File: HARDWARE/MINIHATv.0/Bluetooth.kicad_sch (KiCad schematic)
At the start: 0 parts

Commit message: added BT module and passives+xtals
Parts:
- added C24: 10n, symbol Device:C_Small
- added C25, C26, C27, C28, C29, C30: C_Small, symbol Device:C_Small
- added C31, C32, C33, C34, C35, C36: C, symbol Device:C
- added L1, L2: L, symbol Device:L
- added R26, R27: 4k7, symbol Device:R_Small
- added R28: 1K, symbol Device:R_Small
- added U6: BlueNRG-232NS, Library:VFQFPN-32_5x5_Pitch0.5mm, symbol RFLiB:BlueNRG-232N
- added Y2: 32kHz, symbol Device:Crystal_Small
- added Y3: 32MHz, symbol Device:Crystal_Small
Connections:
- new net: C29.2, U6.18 (FXTAL0), Y3.2
- new net: C27.2, C28.1, L2.1
- new net: R28.1, U6.29 (DIO13)
- new net: C25.1, C26.1, L1.1, U6.27 (SMPSFILT2)
- new net: L1.2, U6.26 (SMPSFILT1)
- new net: R27.2, U6.30 (DIO12)
- new net: C30.2, U6.17 (FXTAL1), Y3.1
- new net: C28.2, U6.22 (SXTAL1), Y2.1
- new net: C27.1, U6.23 (SXTAL0), Y2.2
- new net +3V3: C31.1, C32.1, C33.1, C34.1, R26.1, R27.1, U6.19 (VBAT2), U6.24 (VBAT1), U6.6 (VBAT3)
- new net BOOT: U6.4 (DIO7/BOOT)
- new net BT_RX: U6.3 (DIO8)
- new net BT_TX: U6.32 (DIO11)
- new net BT_VDD1V2: C35.1, C36.1, U6.28 (VDD1V2)
- new net BT_~RST: C24.1, R26.2, U6.25 (RESETN)
- new net GND: C24.2, C25.2, C26.2, C29.1, C30.1, C31.2, C32.2, C33.2, C34.2, C35.2, C36.2, L2.2, R28.2, U6.11 (DIO1), U6.12 (DIO0), U6.15 (ADC1), U6.16 (ADC2), U6.31 (TEST), U6.33 (GND), U6.5 (DIO6), U6.7 (DIO5), U6.8 (DIO4)
- no-connect marks 0 -> 6

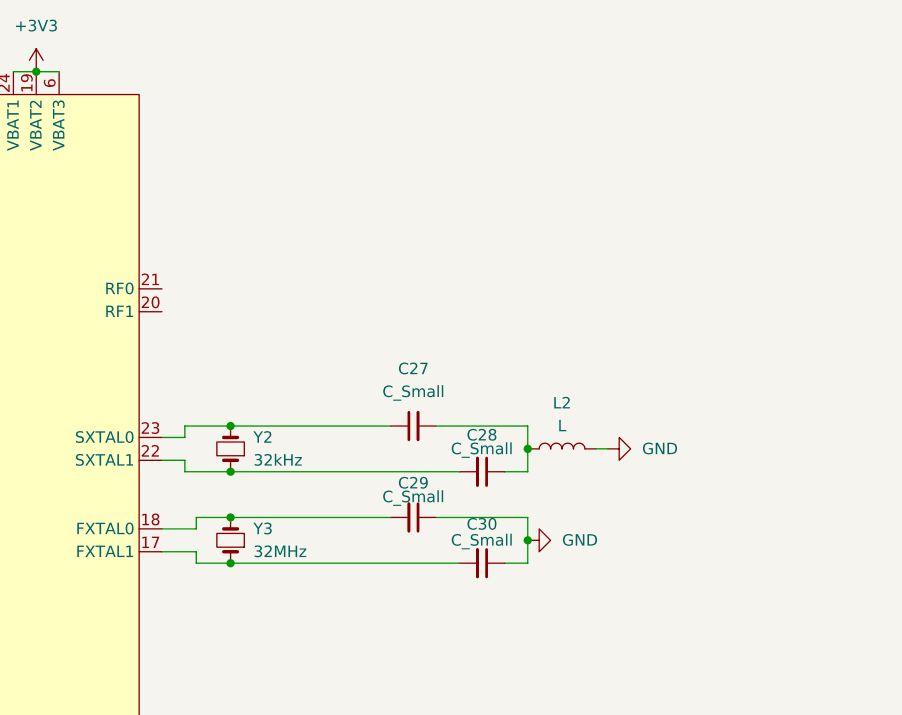
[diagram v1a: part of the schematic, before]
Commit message: passives and filter for BT antenna added to sch
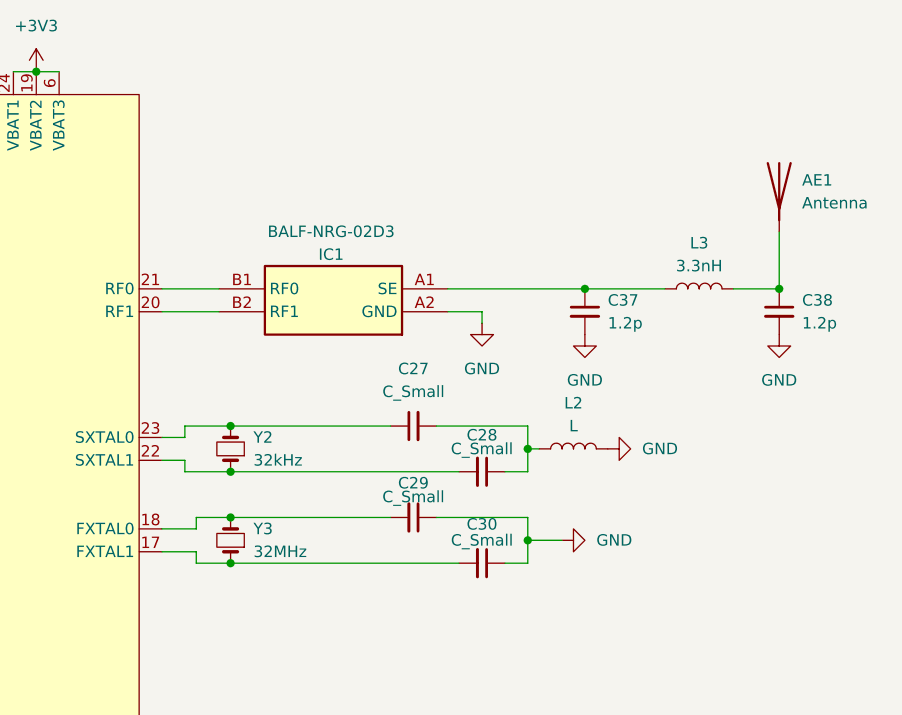
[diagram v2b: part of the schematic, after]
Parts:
- added AE1: Antenna, symbol Device:Antenna
- added C37, C38: 1.2p, Capacitor_SMD:C_0402_1005Metric, symbol Device:C_Small
- added IC1: BALF-NRG-02D3, BALFNRG02D3, symbol tmp:BALF-NRG-02D3
- added L3: 3.3nH, Inductor_SMD:L_0402_1005Metric, symbol Device:L
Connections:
- net GND: now also C37.2, C38.2, IC1.A2 (GND)
- net at U6.20 (RF1): now also IC1.B2 (RF1)
- net at U6.21 (RF0): now also IC1.B1 (RF0)
- new net: AE1.1 (A), C38.1, L3.2
- new net: C37.1, IC1.A1 (SE), L3.1
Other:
- moved on the sheet: L2

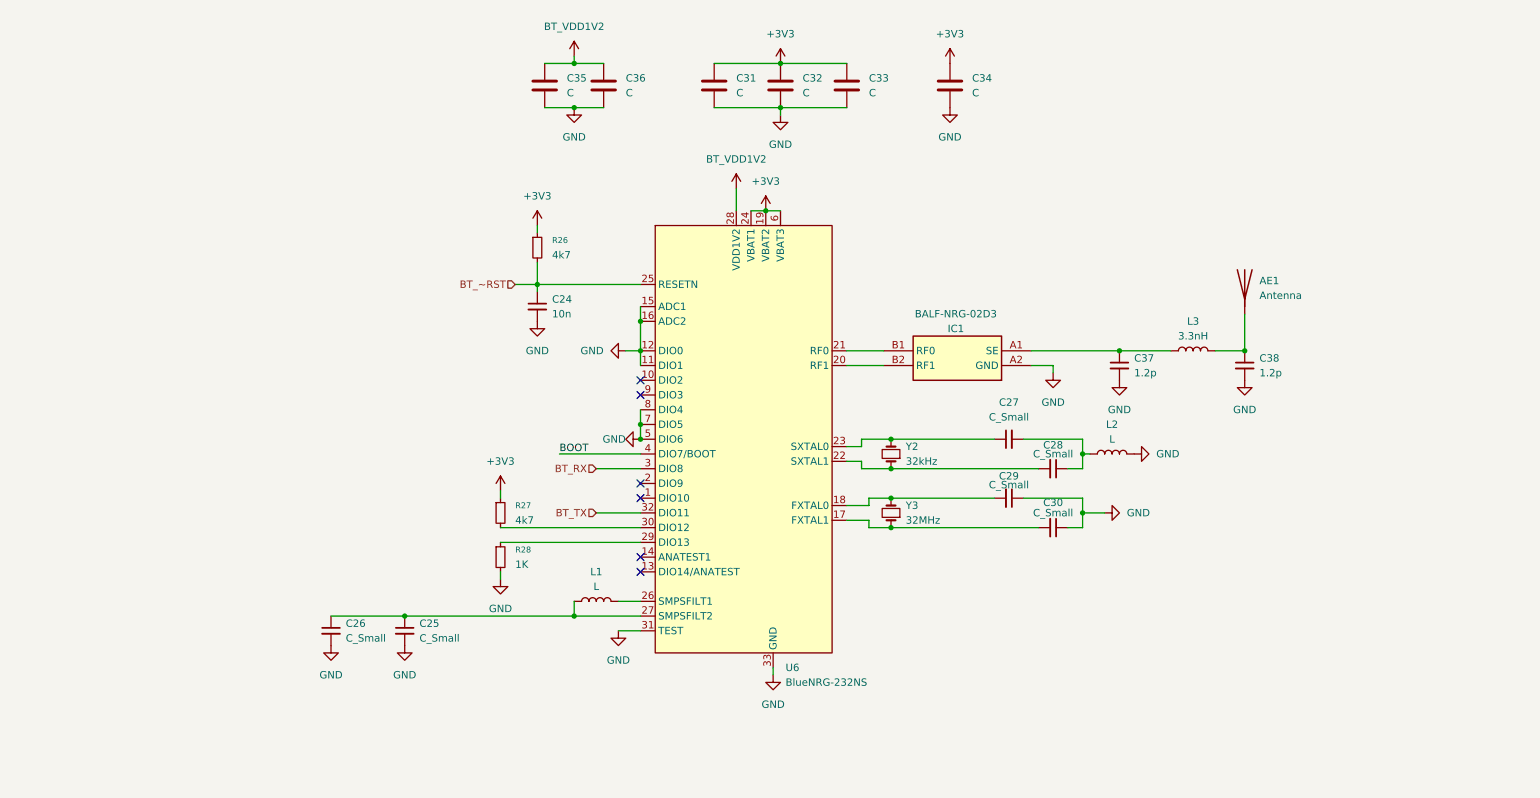
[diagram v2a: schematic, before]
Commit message: added bt chip filter valueas and xtal passives values, added antenna filter sources and footprint
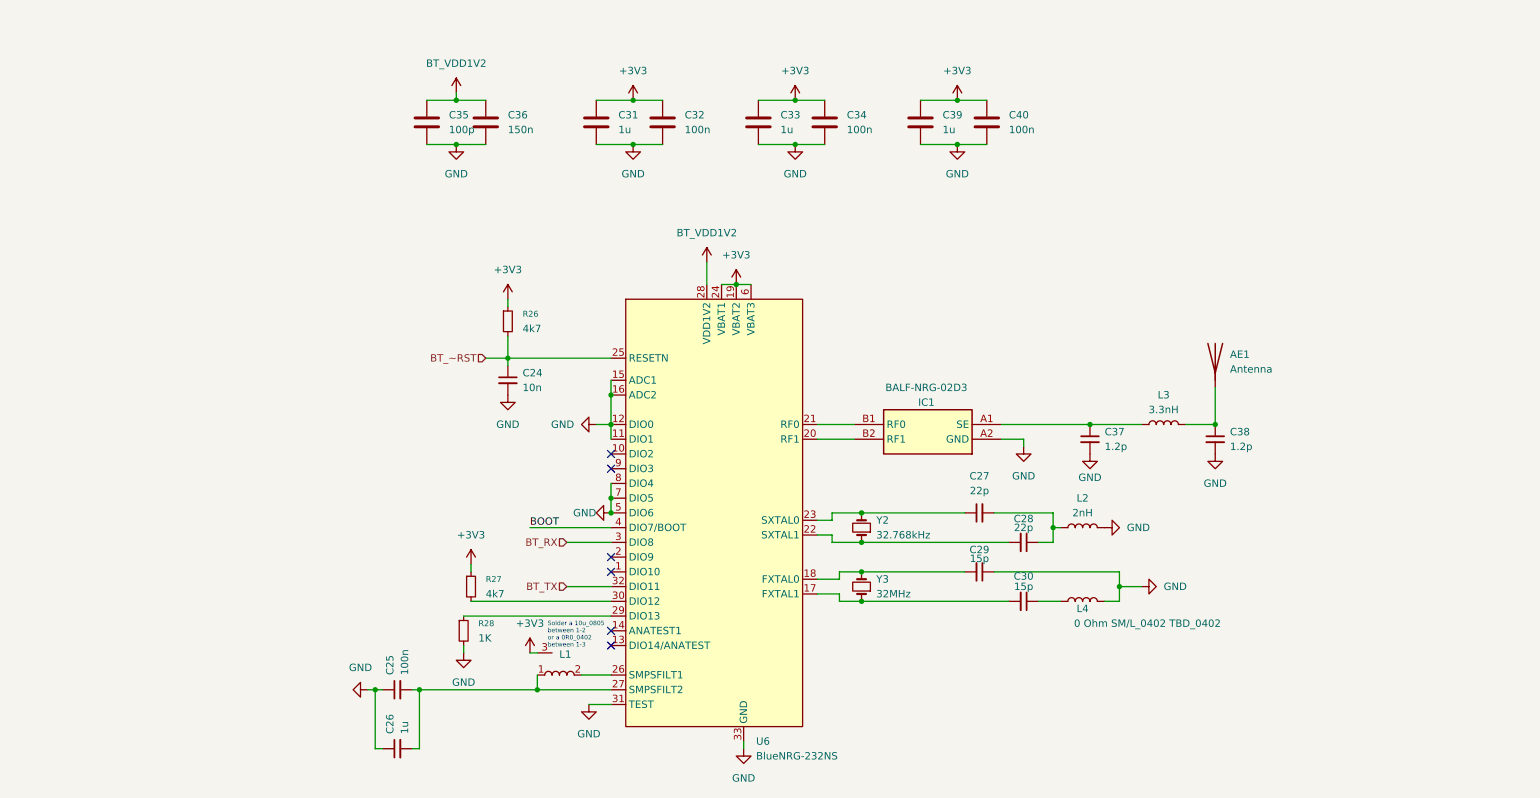
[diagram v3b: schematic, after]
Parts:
- added C39: 1u, symbol Device:C
- added C40: 100n, symbol Device:C
- added L4: 0 Ohm SM/L_0402 TBD_0402, symbol Device:L
- C25: value C_Small -> 100n
- C26: value C_Small -> 1u
- C27, C28: value C_Small -> 22p
- C29, C30: value C_Small -> 15p
- C31, C33: value C -> 1u
- C32, C34: value C -> 100n
- C35: value C -> 100p
- C36: value C -> 150n
- L1: value L -> 10uH; footprint (none) -> LED_SMD:LED_RGB_Lumex_SML-LXT0805SIUGUBW
- L2: value L -> 2nH; footprint (none) -> Inductor_SMD:L_0402_1005Metric
- Y2: value 32kHz -> 32.768kHz
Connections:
- net +3V3: now also L1.3, C39.1, C40.1
- net GND: now also C25.1, C26.1, C39.2, C40.2, L4.2; no longer C25.2, C26.2, C30.1
- net at L1.1, U6.27 (SMPSFILT2): now also C25.2, C26.2; no longer C25.1, C26.1
- new net: C30.1, L4.1
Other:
- note added: "Solder a 10u_0805 between 1-2 or a 0R0_0402 between 1-3"
- moved on the sheet: AE1, C24, C25, C26, C27, C28, C29, C30, C31, C32, C35, C36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

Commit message: boot sw, top page bt added
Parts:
- added J4: Conn_01x02_Pin, symbol Switch:SW_Push
- added R29: 1k, symbol Device:R_Small
- added R30: 4k7, symbol Device:R_Small
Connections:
- net +3V3: now also R29.1
- net BOOT: now also J4.2, R30.1
- net GND: now also R30.2
- new net: J4.1, R29.2
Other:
- moved on the sheet: R28

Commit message: buses defined ind project settings, added stm antenna footprint, organized TOP
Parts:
- AE1: footprint (none) -> RF_Antenna:STM-BLUE-NRG-antenna
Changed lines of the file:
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@@
 	)
 	(junction
+		(at 121.92 85.09)
+		(diameter 0)
+		(color 0 0 0 0)
+	)
+	(junction
 		(at 81.28 138.43)
 		(diameter 0)
@@
 	)
 	(junction
-		(at 121.92 102.87)
-		(diameter 0)
-		(color 0 0 0 0)
-	)
-	(junction
 		(at 165.1 113.03)
 		(diameter 0)
@@
 	(wire
 		(pts
+			(xy 121.92 85.09) (xy 121.92 87.63)
+		)
+		(stroke
+			(width 0)
+			(type default)
+		)
+	)
+	(wire
+		(pts
 			(xy 81.28 133.35) (xy 82.55 133.35)
 		)
@@
 	(wire
 		(pts
-			(xy 121.92 82.55) (xy 121.92 87.63)
+			(xy 121.92 82.55) (xy 121.92 85.09)
 		)
 		(stroke
@@
 	(wire
 		(pts
+			(xy 121.92 100.33) (xy 121.92 102.87)
+		)
+		(stroke
+			(width 0)
+			(type default)
+		)
+	)
+	(wire
+		(pts
 			(xy 160.02 104.14) (xy 160.02 102.87)
 		)
@@
 	(wire
 		(pts
-			(xy 121.92 100.33) (xy 121.92 102.87)
-		)
-		(stroke
-			(width 0)
-			(type default)
-		)
-	)
-	(wire
-		(pts
 			(xy 118.11 135.89) (xy 121.92 135.89)
 		)
@@
 		)
 	)
-	(wire
-		(pts
-			(xy 119.38 87.63) (xy 121.92 87.63)
-		)
-		(stroke
-			(width 0)
-			(type default)
-		)
-	)
 	(label "BOOT"
 		(at 58.42 33.02 180)
@@
 	(symbol
 		(lib_id "power:GND")
-		(at 119.38 87.63 270)
+		(at 121.92 85.09 270)
 		(unit 1)
 		(body_style 1)
@@
 		(fields_autoplaced yes)
 		(property "Reference" "#PWR043"
-			(at 113.03 87.63 0)
+			(at 115.57 85.09 0)
 			(hide yes)
 			(show_name no)
@@
 		)
 		(property "Value" "GND"
-			(at 115.57 87.6299 90)
+			(at 118.11 85.0899 90)
 			(show_name no)
 			(do_not_autoplace no)
@@
 		)
 		(property "Footprint" ""
-			(at 119.38 87.63 0)
+			(at 121.92 85.09 0)
 			(hide yes)
 			(show_name no)
@@
 		)
 		(property "Datasheet" ""
-			(at 119.38 87.63 0)
+			(at 121.92 85.09 0)
 			(hide yes)
 			(show_name no)
@@
 		)
 		(property "Description" "Power symbol creates a global label with name \"GND\" , ground"
-			(at 119.38 87.63 0)
+			(at 121.92 85.09 0)
 			(hide yes)
 			(show_name no)
@@
 	(symbol
 		(lib_id "power:GND")
-		(at 121.92 102.87 270)
+		(at 121.92 100.33 270)
 		(unit 1)
 		(body_style 1)
@@
 		(dnp no)
 		(property "Reference" "#PWR042"
-			(at 115.57 102.87 0)
+			(at 115.57 100.33 0)
 			(hide yes)
 			(show_name no)
@@
 		)
 		(property "Value" "GND"
-			(at 119.38 102.87 90)
+			(at 119.38 100.33 90)
 			(show_name no)
 			(do_not_autoplace no)
@@
 		)
 		(property "Footprint" ""
-			(at 121.92 102.87 0)
+			(at 121.92 100.33 0)
 			(hide yes)
 			(show_name no)
@@
 		)
 		(property "Datasheet" ""
-			(at 121.92 102.87 0)
+			(at 121.92 100.33 0)
 			(hide yes)
 			(show_name no)
@@
 		)
 		(property "Description" "Power symbol creates a global label with name \"GND\" , ground"
-			(at 121.92 102.87 0)
+			(at 121.92 100.33 0)
 			(hide yes)
 			(show_name no)
@@
 			)
 		)
-		(property "Footprint" ""
+		(property "Footprint" "RF_Antenna:STM-BLUE-NRG-antenna"
 			(at 226.06 76.2 0)
 			(hide yes)
@@
 			)
 		)
-		(property "Datasheet" ""
+		(property "Datasheet" "https://www.st.com/resource/en/application_note/an5129-low-cost-pcb-antenna-for-24ghz-radio-meander-design-for-stm32wb-series-stmicroelectronics.pdf"
 			(at 226.06 76.2 0)
 			(hide yes)

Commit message: added i2c for hdmi
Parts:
- added C33: 10n, symbol Device:C_Small
- renumbered C25 to C34, C26 to C35, C35 to C36, C36 to C37, C24 to C38, C31 to C39, C32 to C40, C33 to C41, C34 to C42, C39 to C43, C27 to C44, C29 to C45, C40 to C46, C28 to C47, C30 to C48, C37 to C49, C38 to C50, J4 to J5, L4 to L3, L3 to L4, R29 to R38, R30 to R39, R28 to R40, R27 to R41, R26 to R42, U6 to U7
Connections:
- net BOOT: now also C33.1
- net GND: now also C33.2
- net BT_~RST renamed BT_RSTN

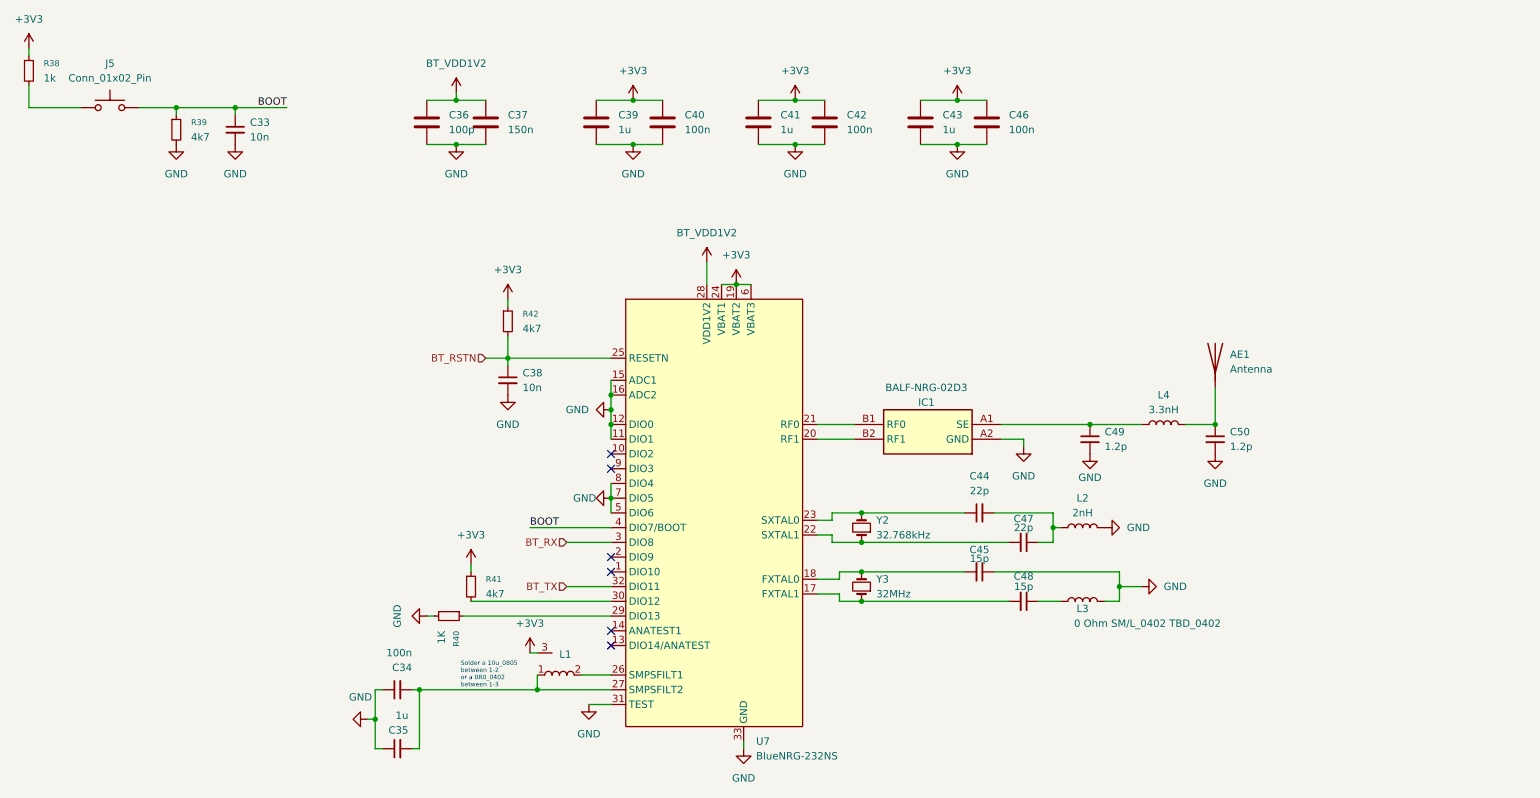
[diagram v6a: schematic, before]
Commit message: BT 1V2 lowdrop added, fdcan pinned to mcu, usb status led added
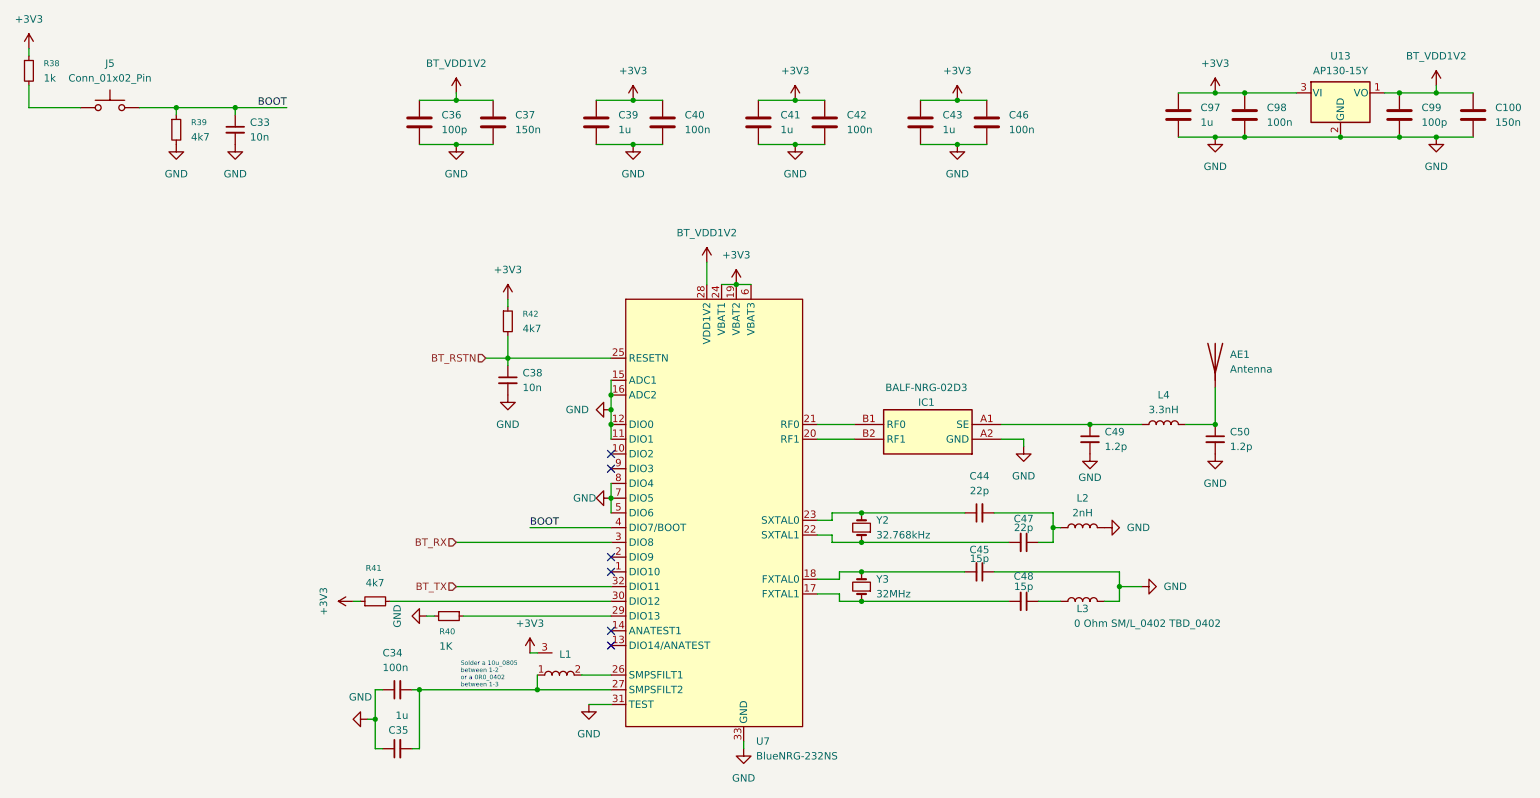
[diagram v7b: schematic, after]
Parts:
- added C100: 150n, symbol Device:C
- added C97: 1u, symbol Device:C
- added C98: 100n, symbol Device:C
- added C99: 100p, symbol Device:C
- added U13: AP130-15Y, Package_TO_SOT_SMD:SOT-89-3, symbol Regulator_Linear:AP130-15Y
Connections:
- net +3V3: now also C97.1, C98.1, U13.3 (VI)
- net BT_VDD1V2: now also C100.1, C99.1, U13.1 (VO)
- net GND: now also C100.2, C97.2, C98.2, C99.2, U13.2 (GND)
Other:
- moved on the sheet: C36, C37, R41
